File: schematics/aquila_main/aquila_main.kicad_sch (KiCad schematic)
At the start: 135 parts

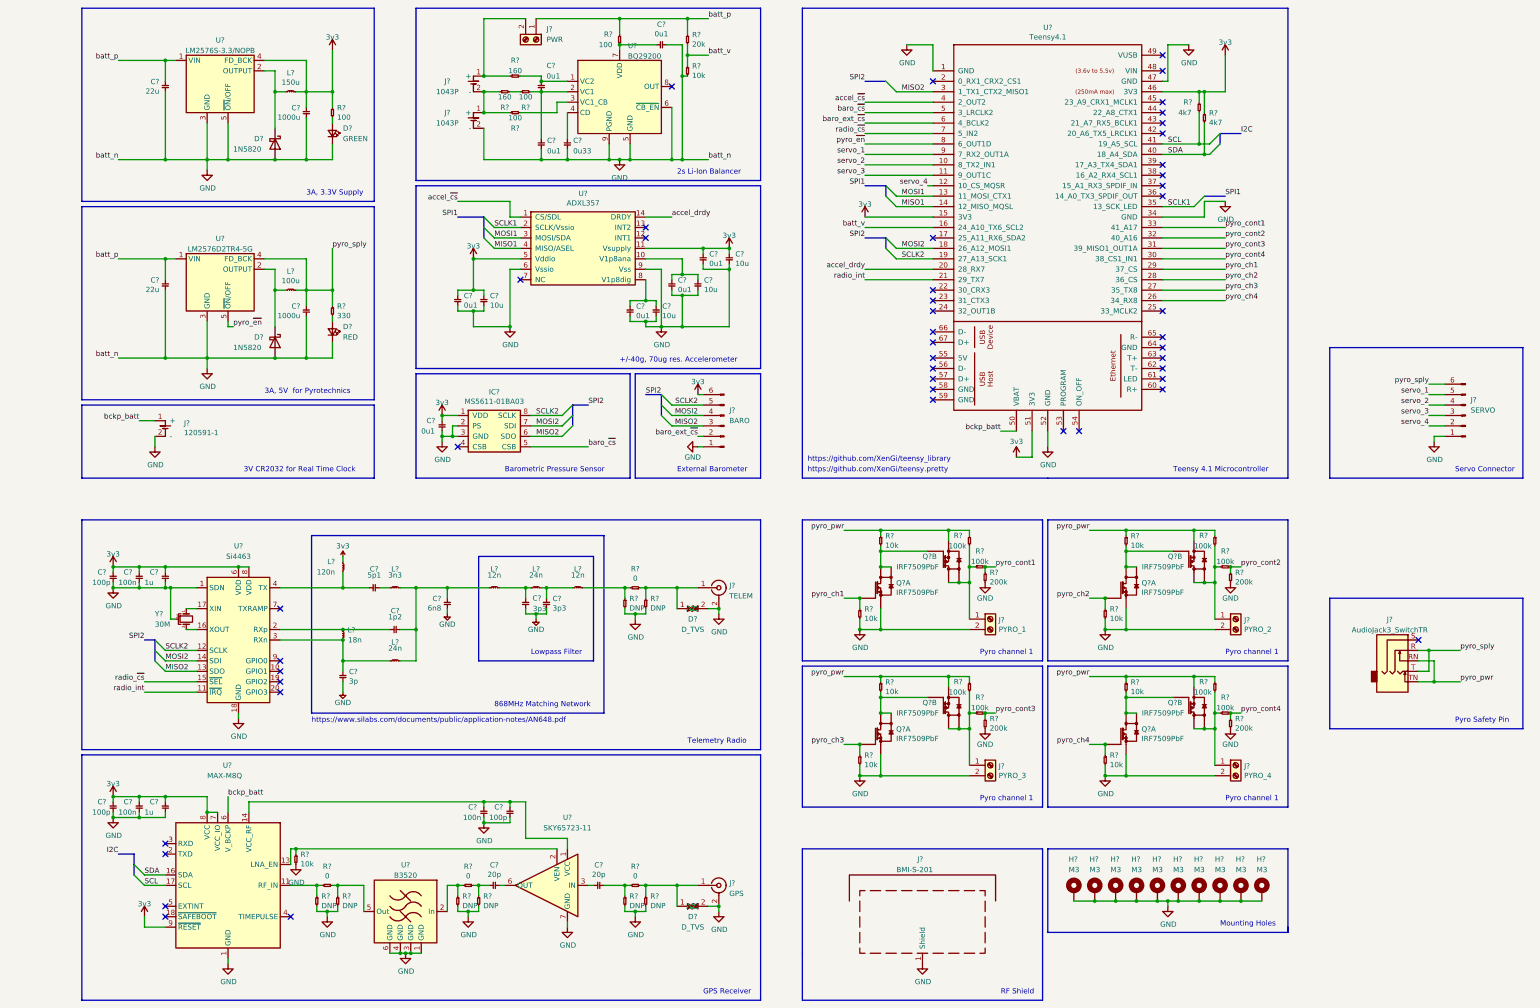
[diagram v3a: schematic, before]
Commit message: assigned all remaining footprints
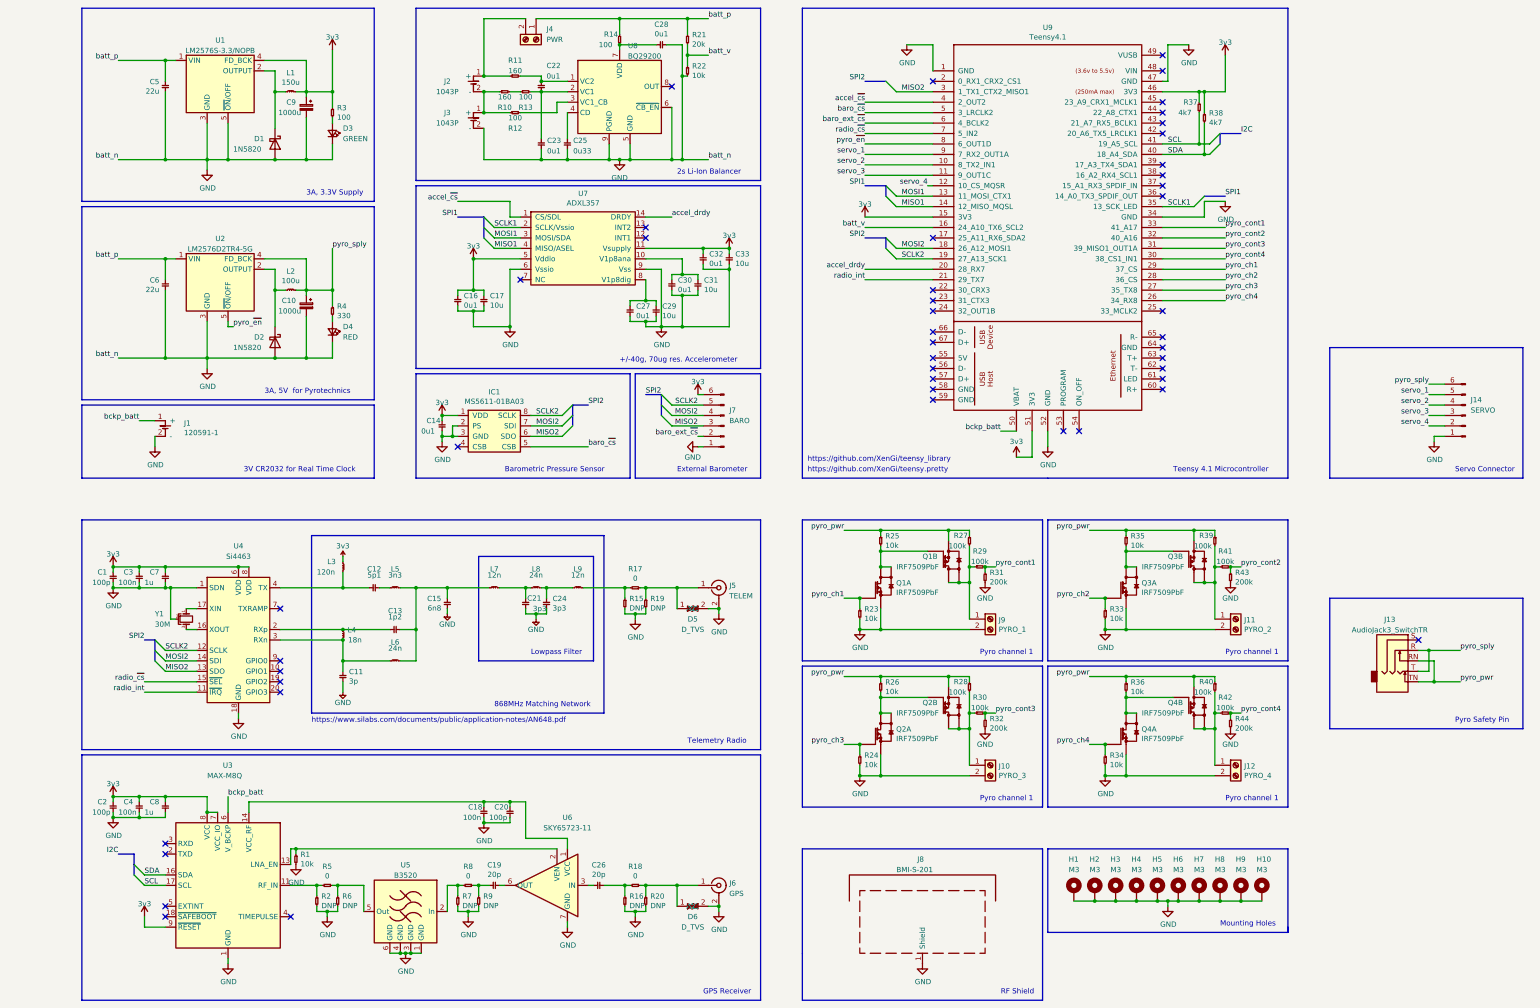
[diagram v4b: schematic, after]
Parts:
- removed C?: 1000u, symbol aquila:C-cusf-kicad
- added C10: 1000u, Capacitor_THT:CP_Radial_D8.0mm_P3.50mm, symbol Device:C_Polarized_Small
- C1, C14, C16, C17, C18, C19, C2, C20, C22, C23, C25, C26, C27, C28, C29, C3, C30, C31, C32, C33, C4, C5, C6, C7, C8: renamed from C?; footprint (none) -> Capacitor_SMD:C_0402_1005Metric
- C11, C12, C13, C15, C21, C24: renamed from C?; footprint Strix:C_0402 -> Capacitor_SMD:C_0402_1005Metric
- C9: renamed from C?; footprint (none) -> Capacitor_THT:CP_Radial_D8.0mm_P3.50mm; symbol aquila:C-cusf-kicad -> Device:C_Polarized_Small; Farnell (none) -> 2760327
- D3: renamed from D?; footprint (none) -> Diode_SMD:D_0603_1608Metric; Farnell (none) -> 3796304
- D4: renamed from D?; footprint (none) -> Diode_SMD:D_0603_1608Metric; Farnell (none) -> 3796306
- J1: renamed from J?; footprint (none) -> aquila:120591-1
- L1: renamed from L?; footprint (none) -> Inductor_THT:L_Toroid_Vertical_L24.6mm_W15.5mm_P11.44mm_Pulse_KM-4; Farnell (none) -> 1209555
- L2: renamed from L?; footprint (none) -> Inductor_THT:L_Toroid_Vertical_L24.6mm_W15.5mm_P11.44mm_Pulse_KM-4; Farnell (none) -> 1209546
- L3, L4, L5, L6, L7, L8, L9: renamed from L?; footprint Strix:L_0402 -> Inductor_SMD:L_0402_1005Metric
- R1, R10, R11, R12, R13, R14, R15, R16, R17, R18, R19, R2, R20, R21, R22, R23, R24, R25, R26, R27, R28, R29, R3, R30, R31, R32, R33, R34, R35, R36, R37, R38, R39, R4, R40, R41, R42, R43, R44, R5, R6, R7, R8, R9: renamed from R?; footprint (none) -> Resistor_SMD:R_0402_1005Metric
- gave numbers to parts that had none: 42
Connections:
- net GND: now also C10.2
- net pyro_sply: now also C10.1

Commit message: preliminary placement of components
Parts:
- L1: value 150u -> 100u; footprint Inductor_THT:L_Toroid_Vertical_L24.6mm_W15.5mm_P11.44mm_Pulse_KM-4 -> aquila:L_MP0028_124_125_127; Farnell 1209555 -> 3370508
- L2: footprint Inductor_THT:L_Toroid_Vertical_L24.6mm_W15.5mm_P11.44mm_Pulse_KM-4 -> aquila:L_MP0028_124_125_127; Farnell 1209546 -> 3370508
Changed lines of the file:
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@@
     (property "Reference" "L2" (id 0) (at 99.06 85.5726 0))
     (property "Value" "100u" (id 1) (at 99.06 87.884 0))
-    (property "Footprint" "Inductor_THT:L_Toroid_Vertical_L24.6mm_W15.5mm_P11.44mm_Pulse_KM-4" (id 2) (at 97.79 90.17 0)
-      (effects (font (size 1.27 1.27)) hide)
-    )
-    (property "Datasheet" "https://www.farnell.com/datasheets/2171927.pdf" (id 3) (at 97.79 90.17 0)
-      (effects (font (size 1.27 1.27)) hide)
-    )
-    (property "Farnell" "1209546" (id 4) (at 97.79 90.17 0)
+    (property "Footprint" "aquila:L_MP0028_124_125_127" (id 2) (at 97.79 90.17 0)
+      (effects (font (size 1.27 1.27)) hide)
+    )
+    (property "Datasheet" "https://www.farnell.com/datasheets/2918522.pdf" (id 3) (at 97.79 90.17 0)
+      (effects (font (size 1.27 1.27)) hide)
+    )
+    (property "Farnell" "3370508" (id 4) (at 97.79 90.17 0)
       (effects (font (size 1.27 1.27)) hide)
     )
@@
     (in_bom yes) (on_board yes)
     (property "Reference" "L1" (id 0) (at 99.06 37.3126 0))
-    (property "Value" "150u" (id 1) (at 99.06 39.624 0))
-    (property "Footprint" "Inductor_THT:L_Toroid_Vertical_L24.6mm_W15.5mm_P11.44mm_Pulse_KM-4" (id 2) (at 97.79 41.91 0)
-      (effects (font (size 1.27 1.27)) hide)
-    )
-    (property "Datasheet" "https://www.farnell.com/datasheets/2171927.pdf" (id 3) (at 97.79 41.91 0)
-      (effects (font (size 1.27 1.27)) hide)
-    )
-    (property "Farnell" "1209555" (id 4) (at 97.79 41.91 0)
+    (property "Value" "100u" (id 1) (at 99.06 39.624 0))
+    (property "Footprint" "aquila:L_MP0028_124_125_127" (id 2) (at 97.79 41.91 0)
+      (effects (font (size 1.27 1.27)) hide)
+    )
+    (property "Datasheet" "https://www.farnell.com/datasheets/2918522.pdf" (id 3) (at 97.79 41.91 0)
+      (effects (font (size 1.27 1.27)) hide)
+    )
+    (property "Farnell" "3370508" (id 4) (at 97.79 41.91 0)
       (effects (font (size 1.27 1.27)) hide)
     )
@@
     )
     (path "/de56e1d2-438f-4de1-963e-76768a4e6948"
-      (reference "L1") (unit 1) (value "150u") (footprint "Inductor_THT:L_Toroid_Vertical_L24.6mm_W15.5mm_P11.44mm_Pulse_KM-4")
+      (reference "L1") (unit 1) (value "100u") (footprint "aquila:L_MP0028_124_125_127")
     )
     (path "/0f4a3645-f36f-453c-bd49-aac924d984e6"
-      (reference "L2") (unit 1) (value "100u") (footprint "Inductor_THT:L_Toroid_Vertical_L24.6mm_W15.5mm_P11.44mm_Pulse_KM-4")
+      (reference "L2") (unit 1) (value "100u") (footprint "aquila:L_MP0028_124_125_127")
     )
     (path "/79bfbd2f-d120-4bb9-b75e-4a2b67982552"

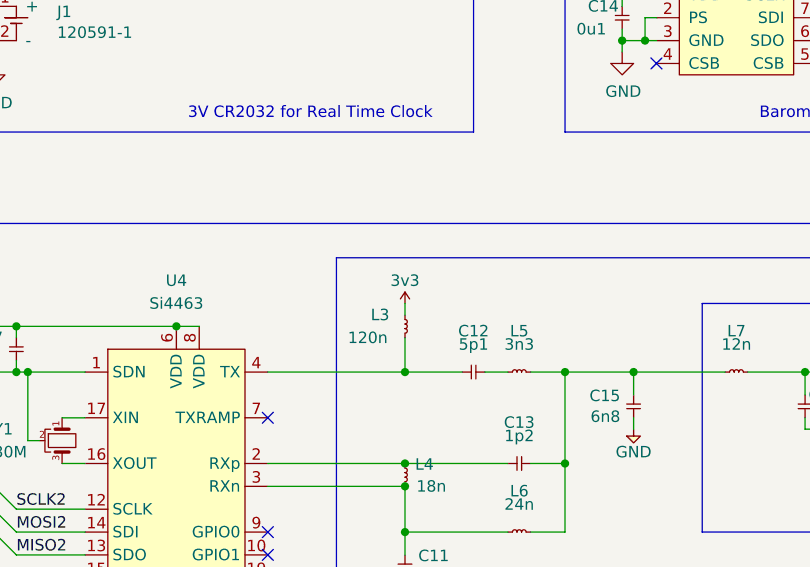
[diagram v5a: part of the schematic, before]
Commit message: placed all components and traces
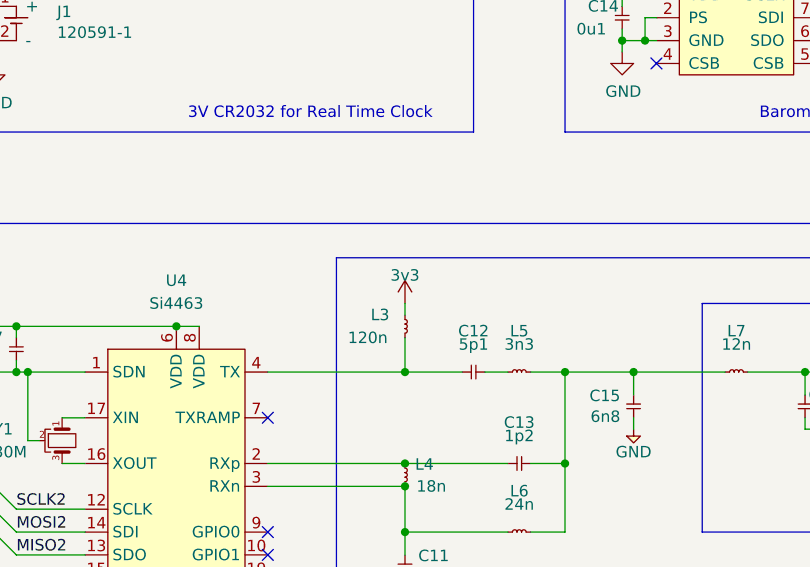
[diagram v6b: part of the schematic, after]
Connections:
- net 3v3 is gone; now on net +3V3: L3.1
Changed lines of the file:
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@@
     (pin "2")
-  )
-  (symbol (lib_id "Strix:3v3") (at 111.76 154.94 0) (unit 1)
-    (in_bom yes) (on_board yes)
-    (property "Reference" "#PWR0137" (id 0) (at 111.76 152.146 0)
-      (effects (font (size 1.27 1.27)) (justify left) hide)
-    )
-    (property "Value" "3v3" (id 1) (at 111.76 152.4 0))
-    (property "Footprint" "" (id 2) (at 111.76 154.94 0)
-      (effects (font (size 1.27 1.27)) hide)
-    )
-    (property "Datasheet" "" (id 3) (at 111.76 154.94 0)
-      (effects (font (size 1.27 1.27)) hide)
-    )
-    (pin "1")
   )
   (symbol (lib_id "Connector:Screw_Terminal_01x02") (at 328.93 205.74 0) (unit 1)
@@
     (pin "1")
     (pin "2")
+  )
+  (symbol (lib_id "power:+3V3") (at 111.76 154.94 0) (unit 1)
+    (in_bom yes) (on_board yes)
+    (property "Reference" "#PWR?" (id 0) (at 111.76 152.146 0)
+      (effects (font (size 1.27 1.27)) (justify left) hide)
+    )
+    (property "Value" "3v3" (id 1) (at 111.76 151.8158 0))
+    (property "Footprint" "" (id 2) (at 111.76 154.94 0)
+      (effects (font (size 1.27 1.27)) hide)
+    )
+    (property "Datasheet" "" (id 3) (at 111.76 154.94 0)
+      (effects (font (size 1.27 1.27)) hide)
+    )
+    (pin "1")
   )
   (symbol (lib_id "aquila:R-cusf-kicad") (at 180.34 165.1 270) (unit 1)
@@
       (reference "#PWR0136") (unit 1) (value "GND") (footprint "")
     )
-    (path "/8c9efe2f-5335-4c8f-83f0-478062b3d361"
-      (reference "#PWR0137") (unit 1) (value "3v3") (footprint "")
-    )
     (path "/cbd06d2a-8a74-4719-b79e-960533a37ec1"
       (reference "#PWR0138") (unit 1) (value "3v3") (footprint "")
@@
       (reference "#PWR0152") (unit 1) (value "GND") (footprint "")
     )
+    (path "/b1f6fb92-0abe-425d-b6e7-ca5f2605cf1a"
+      (reference "#PWR?") (unit 1) (value "3v3") (footprint "")
+    )
     (path "/00000000-0000-0000-0000-0000624707f0"
